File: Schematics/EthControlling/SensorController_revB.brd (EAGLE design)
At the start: 90 x 80 mm, 73 parts, among them IC1 4066D, IC2 MEGA164P/324P/644P-AU, IC3 4066D, IC4 4066D, IC5 4066D, Q1 20.000M

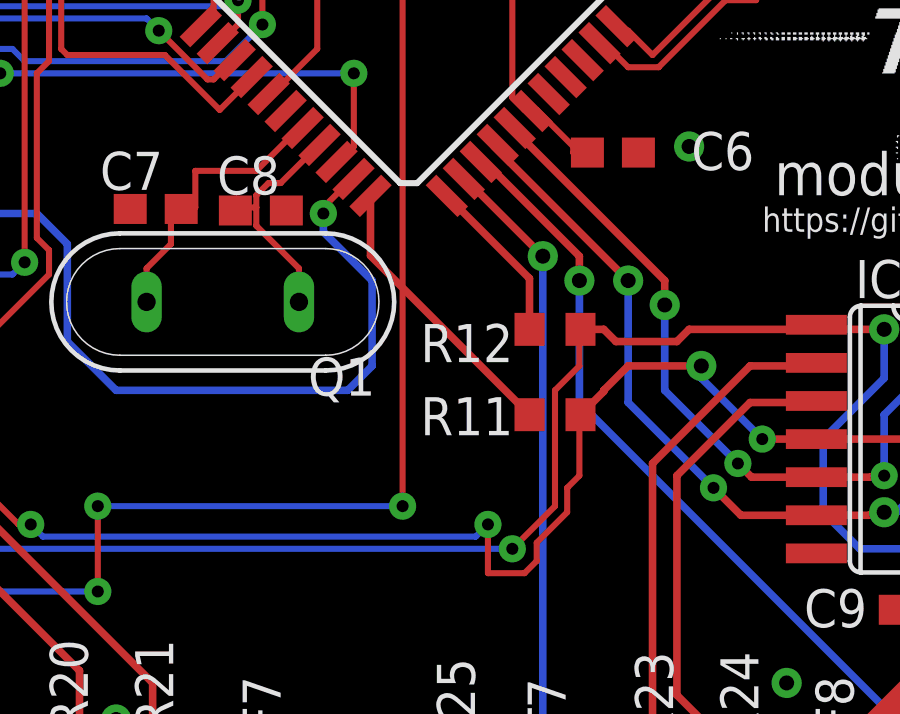
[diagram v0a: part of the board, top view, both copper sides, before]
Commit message: identify schematics by the order number on schematics and submitted gerber files
Signed-off-by: sosoru <siva6991@yahoo.co.jp>
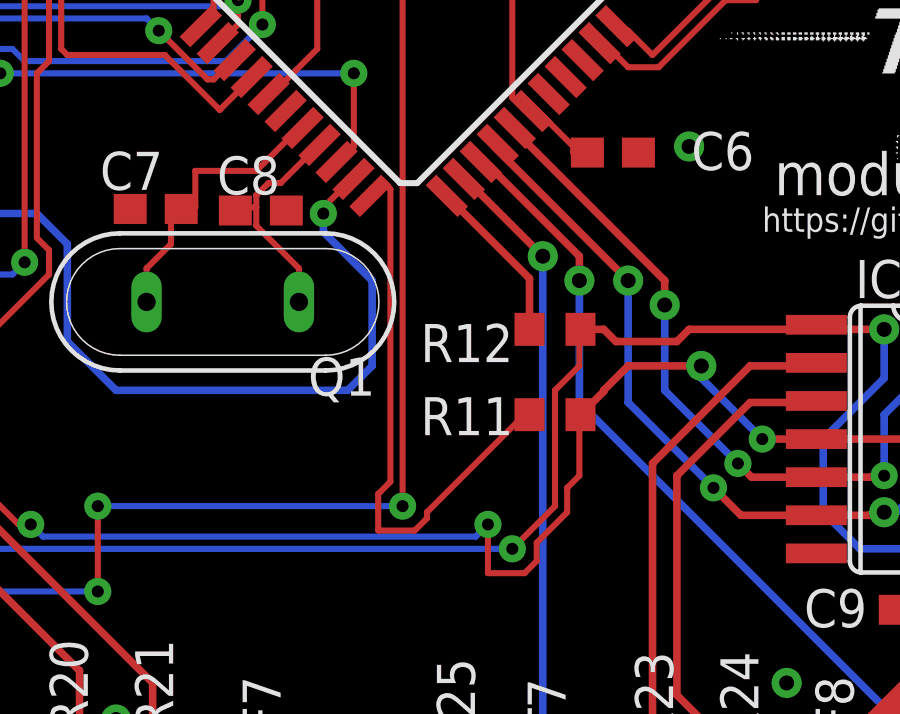
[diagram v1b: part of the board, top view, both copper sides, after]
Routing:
- net N$22: track 9.49 -> 19.2 mm
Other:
- board text added: "D53371"
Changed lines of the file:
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@@
 <text x="58.928" y="34.1376" size="1.4224" layer="25" font="vector" ratio="12">module_SensorControl</text>
 <text x="58.5216" y="32.9184" size="0.8128" layer="25" font="vector">https://github.com/sosoru/TrainUtilizingSystem</text>
+<text x="88.5952" y="69.4944" size="1.778" layer="26" rot="MR0">D53371</text>
 </plain>
 <attributes>
@@
 <contactref element="R11" pad="2"/>
 <contactref element="IC2" pad="11"/>
-<wire x1="45.46320625" y1="34.116753125" x2="45.46320625" y2="32.12199375" width="0.254" layer="1"/>
-<wire x1="45.46320625" y1="32.12199375" x2="50.7628" y2="26.8224" width="0.254" layer="1"/>
+<wire x1="47.3456" y1="23.5712" x2="50.5968" y2="26.8224" width="0.2032" layer="1"/>
+<wire x1="47.3456" y1="23.368" x2="47.3456" y2="23.5712" width="0.2032" layer="1"/>
+<wire x1="46.9392" y1="22.9616" x2="47.3456" y2="23.368" width="0.2032" layer="1"/>
+<wire x1="45.72" y1="22.9616" x2="46.9392" y2="22.9616" width="0.2032" layer="1"/>
+<wire x1="45.72" y1="24.1808" x2="45.72" y2="22.9616" width="0.2032" layer="1"/>
+<wire x1="46.1264" y1="24.5872" x2="45.72" y2="24.1808" width="0.2032" layer="1"/>
+<wire x1="46.1264" y1="34.3408" x2="46.1264" y2="24.5872" width="0.2032" layer="1"/>
+<wire x1="45.9232" y1="34.544" x2="46.1264" y2="34.3408" width="0.2032" layer="1"/>
+<wire x1="45.5168" y1="34.1376" x2="45.9232" y2="34.544" width="0.2032" layer="1"/>
+<wire x1="50.5968" y1="26.8224" x2="50.7628" y2="26.8224" width="0.2032" layer="1"/>
+<wire x1="45.5168" y1="34.1376" x2="45.46320625" y2="34.116753125" width="0.2032" layer="1"/>
 </signal>
 <signal name="N$23">

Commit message: ditto
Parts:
- C3: value (none) -> 100u
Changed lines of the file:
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@@
 <attribute name="VALUE" x="7.9248" y="67.1068" size="1.27" layer="27" ratio="10" rot="R270"/>
 </element>
-<element name="C3" library="rcl" package="E2,5-5" value="" x="18.6944" y="37.7952" rot="R90"/>
+<element name="C3" library="rcl" package="E2,5-5" value="100u" x="18.6944" y="37.7952" rot="R90"/>
 <element name="F3" library="myparts" package="0207/2V" value="POLYSWITCH" x="12.192" y="37.3888" rot="R270"/>
 <element name="C10" library="rcl" package="C1608" value="0.1u" x="25.6032" y="49.9872" smashed="yes">

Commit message: associate of parts of SensorController_revB
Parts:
- T1, T2, T3, T4, T5, T6, T7, T8: value (none) -> BSS138
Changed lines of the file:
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@@
 <attribute name="VALUE" x="52.2478" y="31.5722" size="1.27" layer="27" rot="R180"/>
 </element>
-<element name="T4" library="zetex" package="SOT-23" value="" x="19.9136" y="67.056" smashed="yes" rot="R270">
+<element name="T4" library="zetex" package="SOT-23" value="BSS138" x="19.9136" y="67.056" smashed="yes" rot="R270">
 <attribute name="OC_NEWARK" value="unknown" x="19.9136" y="67.056" size="1.778" layer="27" rot="R270" display="off"/>
 <attribute name="MPN" value="" x="19.9136" y="67.056" size="1.778" layer="27" rot="R270" display="off"/>
@@
 <attribute name="VALUE" x="26.6192" y="67.1068" size="1.27" layer="27" ratio="10" rot="R270"/>
 </element>
-<element name="T1" library="zetex" package="SOT-23" value="" x="38.608" y="67.056" smashed="yes" rot="R270">
+<element name="T1" library="zetex" package="SOT-23" value="BSS138" x="38.608" y="67.056" smashed="yes" rot="R270">
 <attribute name="OC_NEWARK" value="unknown" x="13.4112" y="78.0288" size="1.778" layer="27" rot="R270" display="off"/>
 <attribute name="MPN" value="" x="13.4112" y="78.0288" size="1.778" layer="27" rot="R270" display="off"/>
@@
 <attribute name="VALUE" x="63.1698" y="48.0822" size="1.27" layer="27"/>
 </element>
-<element name="T2" library="zetex" package="SOT-23" value="" x="58.5216" y="67.056" smashed="yes" rot="R270">
+<element name="T2" library="zetex" package="SOT-23" value="BSS138" x="58.5216" y="67.056" smashed="yes" rot="R270">
 <attribute name="OC_NEWARK" value="unknown" x="37.3888" y="78.0288" size="1.778" layer="27" rot="R270" display="off"/>
 <attribute name="MPN" value="" x="37.3888" y="78.0288" size="1.778" layer="27" rot="R270" display="off"/>
@@
 <attribute name="VALUE" x="64.8208" y="67.1068" size="1.27" layer="27" ratio="10" rot="R270"/>
 </element>
-<element name="T3" library="zetex" package="SOT-23" value="" x="76.8096" y="67.056" smashed="yes" rot="R270">
+<element name="T3" library="zetex" package="SOT-23" value="BSS138" x="76.8096" y="67.056" smashed="yes" rot="R270">
 <attribute name="OC_NEWARK" value="unknown" x="19.5072" y="81.6864" size="1.778" layer="27" rot="R270" display="off"/>
 <attribute name="MPN" value="" x="19.5072" y="81.6864" size="1.778" layer="27" rot="R270" display="off"/>
@@
 </element>
 <element name="C5" library="rcl" package="C1608" value="0.1u" x="25.1968" y="19.9136"/>
-<element name="T5" library="zetex" package="SOT-23" value="" x="14.6304" y="13.8176" smashed="yes" rot="R90">
+<element name="T5" library="zetex" package="SOT-23" value="BSS138" x="14.6304" y="13.8176" smashed="yes" rot="R90">
 <attribute name="OC_NEWARK" value="unknown" x="35.7632" y="2.8448" size="1.778" layer="27" rot="R90" display="off"/>
 <attribute name="MPN" value="" x="35.7632" y="2.8448" size="1.778" layer="27" rot="R90" display="off"/>
@@
 <attribute name="VALUE" x="44.5008" y="13.7668" size="1.27" layer="27" ratio="10" rot="R90"/>
 </element>
-<element name="T6" library="zetex" package="SOT-23" value="" x="32.512" y="13.8176" smashed="yes" rot="R90">
+<element name="T6" library="zetex" package="SOT-23" value="BSS138" x="32.512" y="13.8176" smashed="yes" rot="R90">
 <attribute name="OC_NEWARK" value="unknown" x="89.8144" y="-0.8128" size="1.778" layer="27" rot="R90" display="off"/>
 <attribute name="MPN" value="" x="89.8144" y="-0.8128" size="1.778" layer="27" rot="R90" display="off"/>
@@
 <attribute name="VALUE" x="63.1698" y="18.415" size="1.27" layer="27"/>
 </element>
-<element name="T7" library="zetex" package="SOT-23" value="" x="51.6128" y="13.8176" smashed="yes" rot="R90">
+<element name="T7" library="zetex" package="SOT-23" value="BSS138" x="51.6128" y="13.8176" smashed="yes" rot="R90">
 <attribute name="OC_NEWARK" value="unknown" x="72.7456" y="2.8448" size="1.778" layer="27" rot="R90" display="off"/>
 <attribute name="MPN" value="" x="72.7456" y="2.8448" size="1.778" layer="27" rot="R90" display="off"/>
@@
 <attribute name="VALUE" x="81.4832" y="13.7668" size="1.27" layer="27" ratio="10" rot="R90"/>
 </element>
-<element name="T8" library="zetex" package="SOT-23" value="" x="69.9008" y="13.8176" smashed="yes" rot="R90">
+<element name="T8" library="zetex" package="SOT-23" value="BSS138" x="69.9008" y="13.8176" smashed="yes" rot="R90">
 <attribute name="OC_NEWARK" value="unknown" x="127.2032" y="-0.8128" size="1.778" layer="27" rot="R90" display="off"/>
 <attribute name="MPN" value="" x="127.2032" y="-0.8128" size="1.778" layer="27" rot="R90" display="off"/>
